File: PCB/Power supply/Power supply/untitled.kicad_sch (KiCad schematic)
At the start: 32 parts, among them Q1 BD140, Q2 BD139, U5 L7812, U6 LM317_TO-220, U7 L7912, U8 LM337_TO220

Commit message: Made Power Supply schematic prettier
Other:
- note added: "TIP35C ON EXTERNAL HEATSINK"
- note added: "TIP36C ON EXTERNAL HEATSINK"
- note removed: "TIP35C on external heatsink"
- note removed: "TIP36C on external heatsink"
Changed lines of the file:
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@@
 		)
 	)
-	(text "TIP36C on external heatsink"
+	(text "TIP36C ON EXTERNAL HEATSINK"
 		(exclude_from_sim no)
-		(at 76.708 190.754 0)
+		(at 79.756 189.738 0)
 		(effects
 			(font
+				(face "AIGDT")
 				(size 1.5 1.5)
 				(thickness 0.6)
@@
 		)
 	)
-	(text "TIP35C on external heatsink"
+	(text "TIP35C ON EXTERNAL HEATSINK\n"
 		(exclude_from_sim no)
-		(at 76.454 25.146 0)
+		(at 77.216 28.448 0)
 		(effects
 			(font
+				(face "AIGDT")
 				(size 1.5 1.5)
 				(thickness 0.6)
@@
 		(effects
 			(font
+				(face "AIGDT")
 				(size 3 3)
 				(thickness 0.6)
@@
 	(text "12V REGULATOR"
 		(exclude_from_sim no)
-		(at 222.25 20.32 0)
+		(at 233.426 23.368 0)
 		(effects
 			(font
+				(face "AIGDT")
 				(size 3 3)
 				(thickness 0.6)

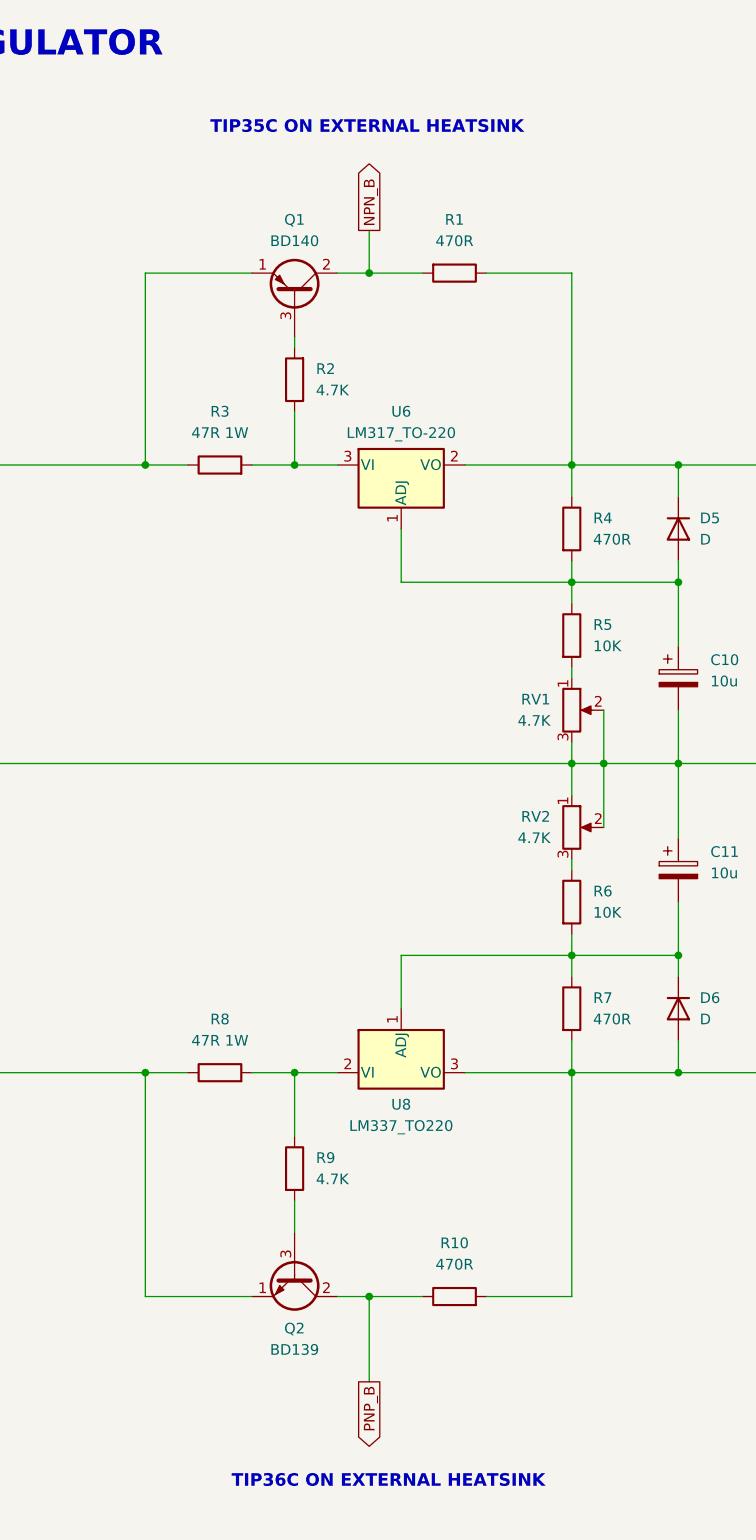
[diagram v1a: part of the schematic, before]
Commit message: Did some simulations, fixed some mistakes in PSU schematic
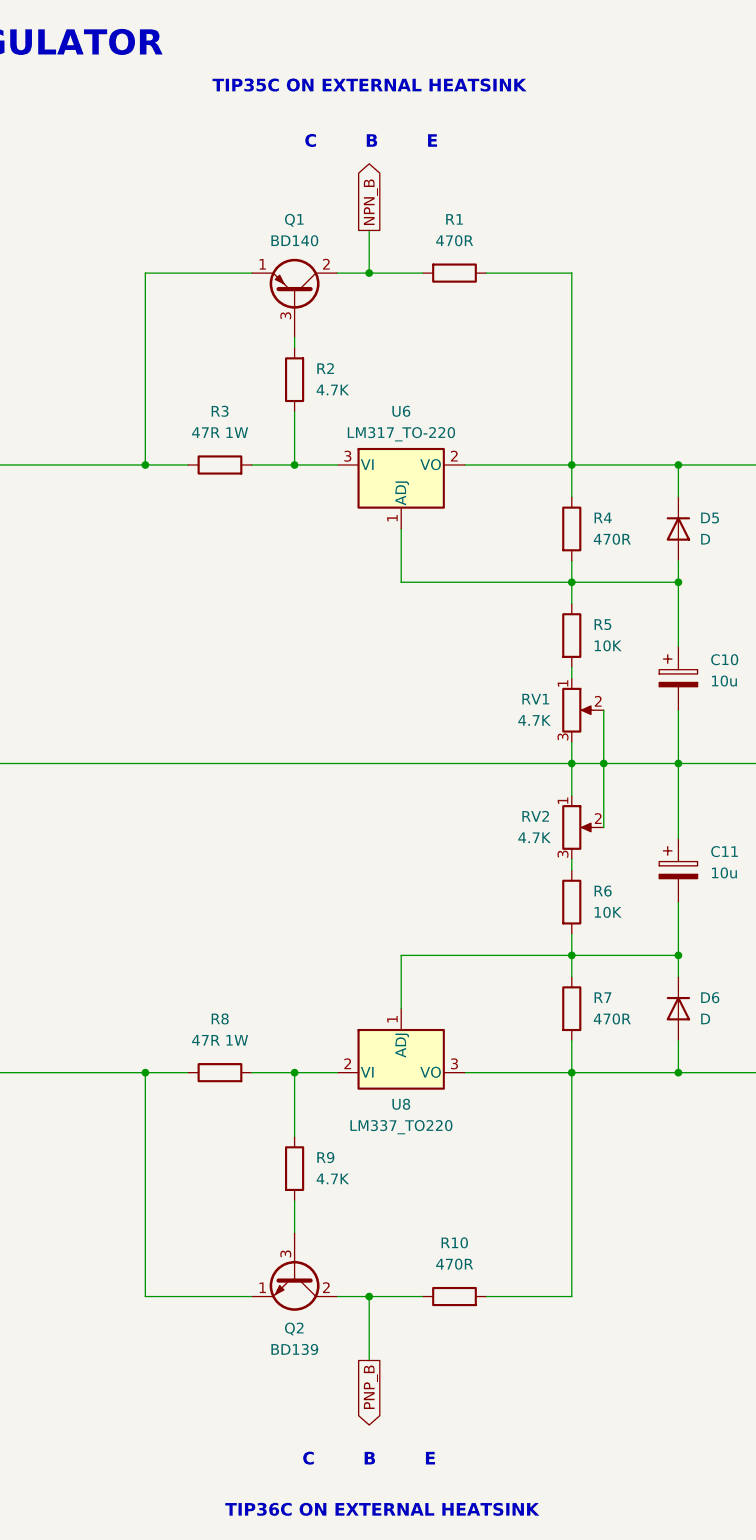
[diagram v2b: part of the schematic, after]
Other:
- note added: "C B E"
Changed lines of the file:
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@@
 	(wire
 		(pts
-			(xy 77.47 167.64) (xy 77.47 177.8)
+			(xy 77.47 167.64) (xy 77.47 175.26)
 		)
 		(stroke
@@
 		)
 	)
-	(text "TIP36C ON EXTERNAL HEATSINK"
+	(text "C        B        E\n"
 		(exclude_from_sim no)
-		(at 79.756 189.738 0)
+		(at 77.47 187.198 0)
 		(effects
 			(font
@@
 		)
 	)
+	(text "TIP36C ON EXTERNAL HEATSINK"
+		(exclude_from_sim no)
+		(at 78.994 193.294 0)
+		(effects
+			(font
+				(face "AIGDT")
+				(size 1.5 1.5)
+				(thickness 0.6)
+				(bold yes)
+				(color 0 0 0 1)
+			)
+		)
+	)
 	(text "TIP35C ON EXTERNAL HEATSINK\n"
 		(exclude_from_sim no)
-		(at 77.216 28.448 0)
+		(at 77.47 23.622 0)
 		(effects
 			(font
@@
 		)
 	)
+	(text "C        B        E\n"
+		(exclude_from_sim no)
+		(at 77.724 30.226 0)
+		(effects
+			(font
+				(face "AIGDT")
+				(size 1.5 1.5)
+				(thickness 0.6)
+				(bold yes)
+				(color 0 0 0 1)
+			)
+		)
+	)
 	(global_label "NPN_B"
 		(shape output)
@@
 	(global_label "PNP_B"
 		(shape output)
-		(at 77.47 177.8 270)
+		(at 77.47 175.26 270)
 		(fields_autoplaced yes)
 		(effects
@@
 		)
 		(property "Intersheetrefs" "${INTERSHEET_REFS}"
-			(at 77.47 186.8933 90)
+			(at 77.47 184.3533 90)
 			(effects
 				(font
